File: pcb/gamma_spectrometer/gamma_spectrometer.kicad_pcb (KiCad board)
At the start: 2 copper layers, 255 x 45 mm, 232 parts, among them J101 DX07S024WJ3R400, Q201 IRLML0040, Q401 MMBTA42, Q402 MMBTA42, Q403 MMBTA42, T201 ATB322524-0110-T000, U101 LP5907MFX-3.3, U102 AMS1117-3.3, U103 FT231XQ, U104 TPS60400DBV, U201 max1847eee+, U202 TL431, U301 REF35250QDBVR, U302 STM32G474MET6, U303 W25Q64JVSSIQ, U402 ADA4817-1ARDZ, Y301 ABM8G-16.000MHZ-4Y-T3

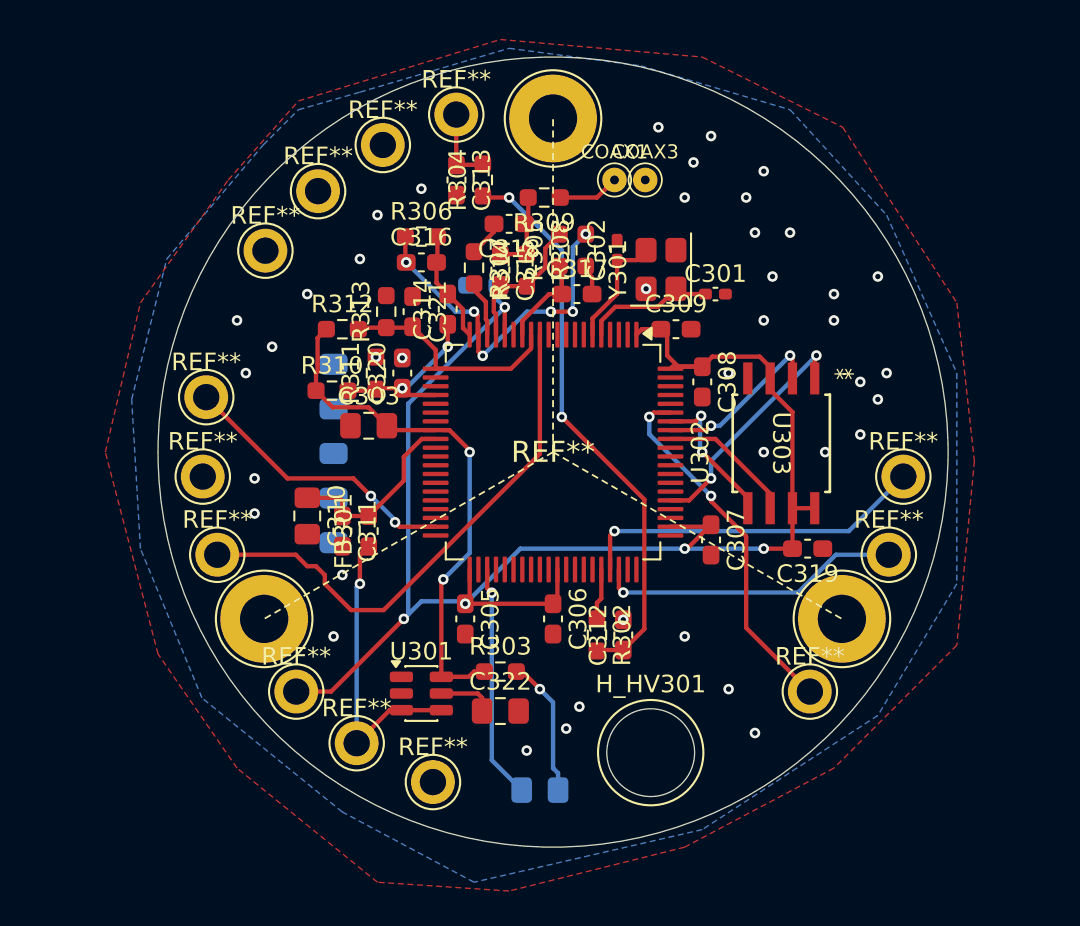
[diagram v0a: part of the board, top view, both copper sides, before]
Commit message: pcb: земля МК подключена, C320 удалён, C314/C317 → 1 мкФ, SWD-пятаки убраны
Плата МК:
- все GND-выводы U302 подключены (15, 27/VSSA, 40, 50 висели);
  зона GND на F.Cu: зазор 0.5 → 0.25 мм, зазор термобарьера → 0.2 мм;
  GND-виа 41 → 97. Остаётся: выводы 50 и 61 на одной спице (starved_thermal).
- TP_SWD301 удалён: прошивка — проводами к выводам 63/64/7 U302.

Схема МК (ревью REVIEW_critic_2026-09-15, находки 1.1 и 1.3, вариант V2):
- C320 удалён (100 нФ на PB0 делил сигнал ×0.5 вместе с C314);
- C314, C317: 100 нФ → 1 мкФ (CC0603JRX7R7BB105), τ связей ~1 мс.

USB-плата: J101 на проектной копии футпринта USB-C (экран на GND).

Co-Authored-By: Claude Opus 5 (1M context) <noreply@anthropic.com>
Claude-Session: https://claude.ai/code/session_018uEKxzknn1WsQbGcTkkQF5
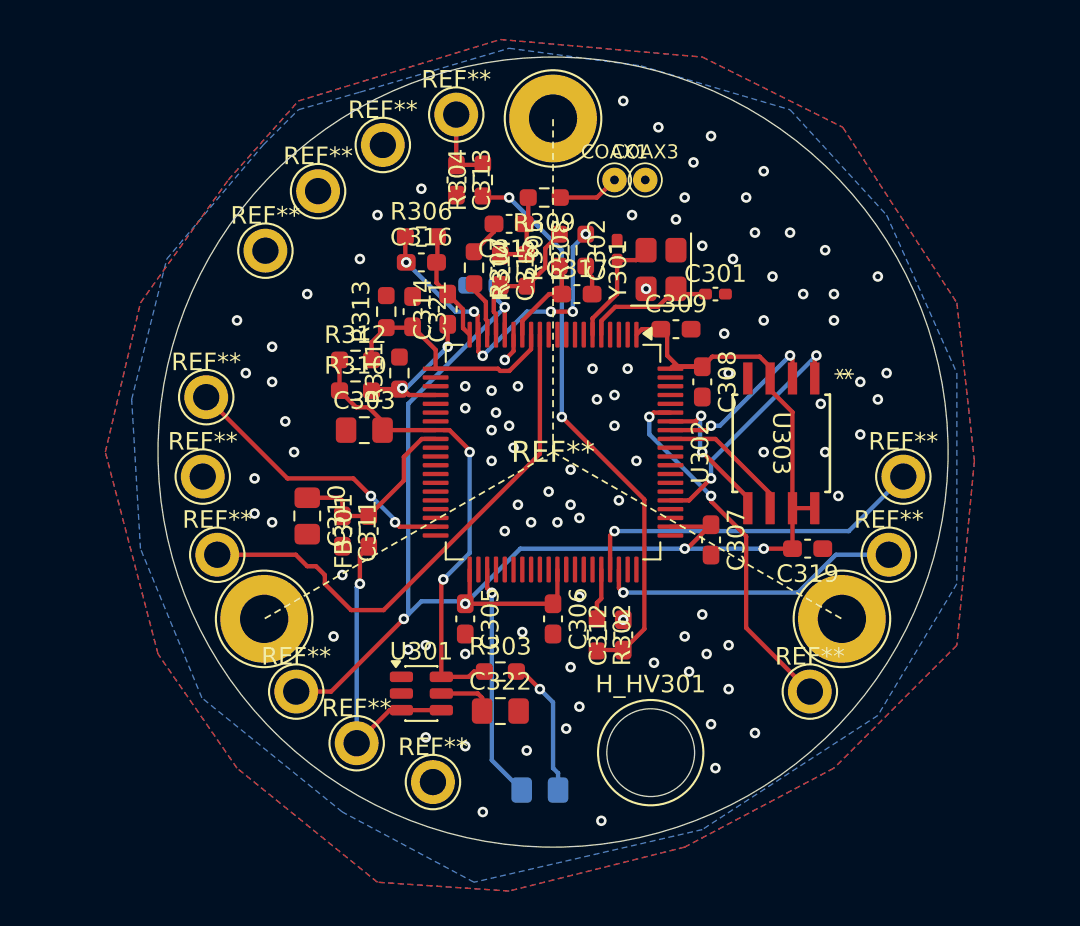
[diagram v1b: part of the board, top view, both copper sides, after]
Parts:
- removed C320: 0.1uF, Capacitor_SMD:C_0603_1608Metric_Pad1.08x0.95mm_HandSolder
- removed TP_SWD301: TP_SWD_5x0805, TP_SWD_5x0805
- C314, C317: value 0.1uF -> 1uF
- moved R312 1.90 mm to (228.8, 94.8)
- moved R310 1.34 mm to (228.8, 96.5)
- moved R311 1.34 mm to (231.2, 95.5)
- moved C303 0.35 mm to (229.2, 98.8)
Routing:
- net Net-(U301-VREF): track 29.6 -> 26.6 mm
- net GND: track 16.9 -> 18.6 mm, vias 98 -> 152
- net Net-(U302-PB0): track 10.4 -> 9.03 mm
- net Net-(U302-PA1): track 12.8 -> 13.5 mm

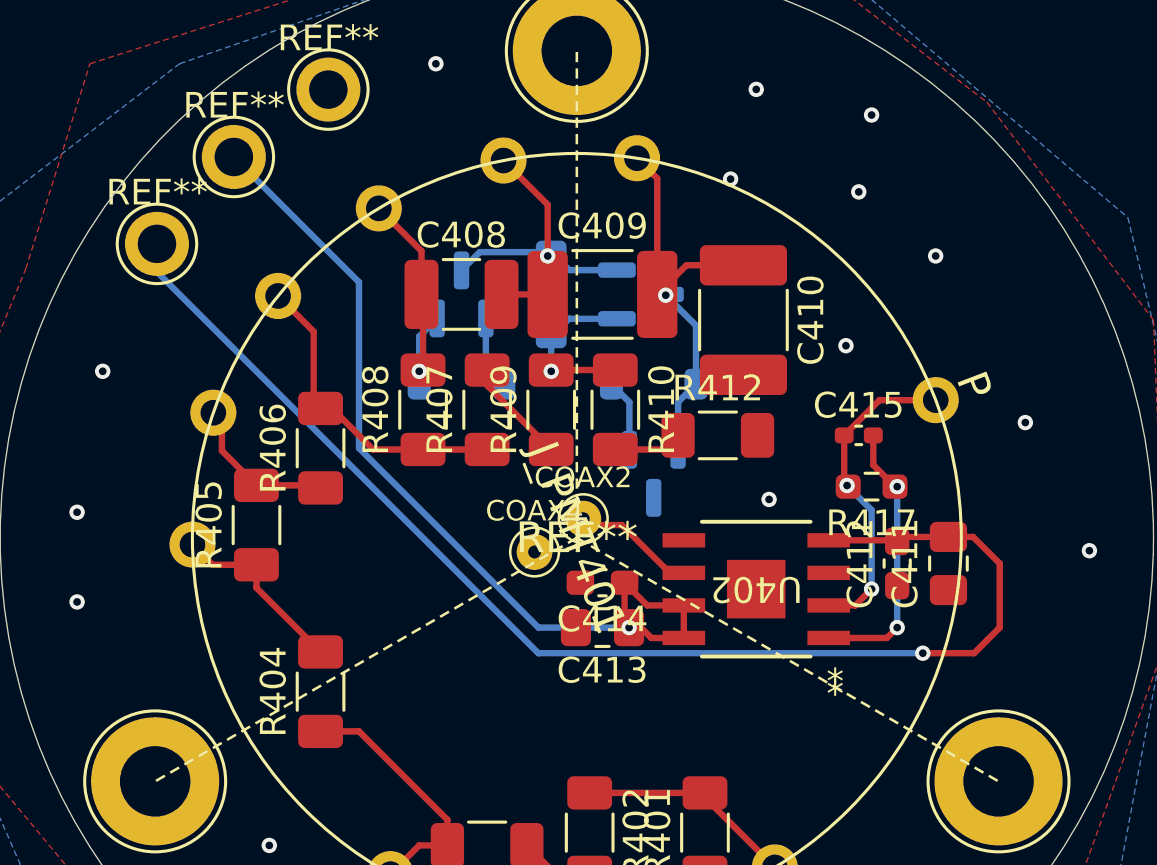
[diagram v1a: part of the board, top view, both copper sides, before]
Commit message: pcb: делитель — R411 22 Ом на выходе TIA, +IN U402 на земле, обратная связь короче
- R411 = 22 Ом (RC0402FR-0722RL, 0402) между выводом 6 U402 и AMP_OUT, вплотную к
  выводу: R_SNUB против генерации TIA на ёмкостную нагрузку (кабель + вход шейпера).
- Вывод 3 U402 (+IN, опорная земля TIA) не был подключён — виа в паде на GND B.Cu.
- R417/C415 перенесены к выводам 1–2: петля обратной связи короче,
  паразитная C(анод↔FB) 0.13–0.22 → 0.05–0.09 пФ.
- Заливка перезалита; DRC по делителю: 0 нарушений зазора, схема↔плата 0.

Co-Authored-By: Claude Opus 5 (1M context) <noreply@anthropic.com>
Claude-Session: https://claude.ai/code/session_018uEKxzknn1WsQbGcTkkQF5
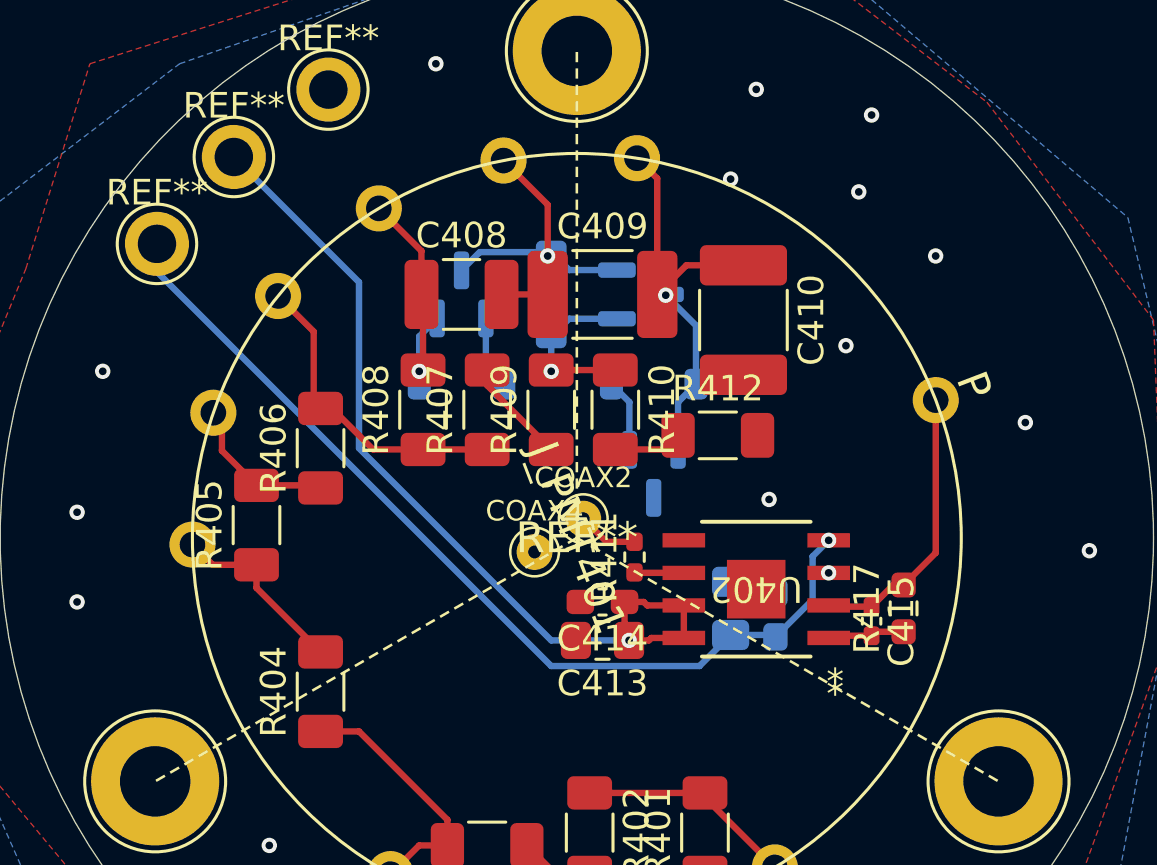
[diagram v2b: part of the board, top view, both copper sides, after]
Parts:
- added R411: 22, Resistor_SMD:R_0402_1005Metric_Pad0.72x0.64mm_HandSolder, F.Cu at (312.2, 100.8)
- C411, C412: moved to B.Cu
- moved C411 8.68 mm to (316.0, 102.8), turned to -90 degrees
- moved C415 7.27 mm to (321.5, 103.2), turned to -90 degrees
- moved C412 5.15 mm to (317.8, 103.0), turned to -90 degrees
- moved R417 4.91 mm to (322.8, 102.8), turned to 90 degrees
- moved C414 0.75 mm to (311.0, 102.5)
- moved C413 0.50 mm to (311.0, 104.0)
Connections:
- U402 pad 6: AMP_OUT -> Net-(U402-OUT)
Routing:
- net −5V_A: track 63.7 -> 50.3 mm
- net FeedBack: track 10.7 -> 3.02 mm, vias 2 -> 0
- net AMP_OUT: track 8.30 -> 5.88 mm
- net Net-(U402-OUT): track 0.00 -> 1.93 mm
- net /Divider_Board/P: track 12.6 -> 11.0 mm, vias 2 -> 0
- net GND: vias 152 -> 153

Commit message: pcb: Q201 IRLML0040 → IRLML0060 (60 В) — запас по выбросу стока
Ключ обратноходового преобразователя ВВ-платы: та же посадка SOT-23 и
распиновка (1-G, 2-S, 3-D). Пик на стоке по расчёту 38.8 В типично,
43–45 В в худшем случае — у IRLML0040 (40 В, лавина не нормирована)
запаса не было. Снаббер BAS516 + C208 + 2×BZT52C18 без изменений.
Схема↔плата: 0 расхождений.

Co-Authored-By: Claude Opus 5 (1M context) <noreply@anthropic.com>
Claude-Session: https://claude.ai/code/session_018uEKxzknn1WsQbGcTkkQF5
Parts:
- Q201: value IRLML0040 -> IRLML0060
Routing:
- net GND: vias 153 -> 164
- net (no net): vias 0 -> 1
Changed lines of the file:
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@@
 			)
 		)
-		(property "Value" "IRLML0040"
+		(property "Value" "IRLML0060"
 			(at 0 2.4 0)
 			(layer "F.Fab")
@@
 			)
 		)
-		(property "PN" "IRLML0040"
+		(property "PN" "IRLML0060"
 			(at 0 0 0)
 			(unlocked yes)
@@
 			)
 		)
-		(property "Ссылка на покупку " "https://www.electronshik.ru/item/HOTTECH/IRLML0040"
+		(property "Ссылка на покупку " "https://www.electronshik.ru/item/HOTTECH/IRLML0060"
 			(at 0 0 0)
 			(unlocked yes)
@@
 		(layer "Edge.Cuts")
 	)
+	(via
+		(at 137.5 118)
+		(size 0.6)
+		(drill 0.3)
+		(layers "F.Cu" "B.Cu")
+		(net 0)
+	)
 	(segment
 		(start 173.3625 93)
@@
 	)
 	(via
+		(at 321.25 96.5)
+		(size 0.6)
+		(drill 0.3)
+		(layers "F.Cu" "B.Cu")
+		(free yes)
+		(net 3)
+	)
+	(via
 		(at 173.5 79)
 		(size 0.6)
@@
 	)
 	(via
+		(at 322 106.5)
+		(size 0.6)
+		(drill 0.3)
+		(layers "F.Cu" "B.Cu")
+		(free yes)
+		(net 3)
+	)
+	(via
 		(at 241 112.25)
 		(size 0.6)
@@
 	)
 	(via
+		(at 319.75 105.75)
+		(size 0.6)
+		(drill 0.3)
+		(layers "F.Cu" "B.Cu")
+		(free yes)
+		(net 3)
+	)
+	(via
 		(at 93 115)
 		(size 0.6)
@@
 	)
 	(via
+		(at 304.75 85)
+		(size 0.6)
+		(drill 0.3)
+		(layers "F.Cu" "B.Cu")
+		(free yes)
+		(net 3)
+	)
+	(via
 		(at 238.25 110.25)
 		(size 0.6)
@@
 	)
 	(via
+		(at 310 84.75)
+		(size 0.6)
+		(drill 0.3)
+		(layers "F.Cu" "B.Cu")
+		(free yes)
+		(net 3)
+	)
+	(via
 		(at 164.5 102)
 		(size 0.6)
@@
 	)
 	(via
+		(at 304.25 102)
+		(size 0.6)
+		(drill 0.3)
+		(layers "F.Cu" "B.Cu")
+		(free yes)
+		(net 3)
+	)
+	(via
 		(at 166 108)
 		(size 0.6)
@@
 	)
 	(via
+		(at 305 103.75)
+		(size 0.6)
+		(drill 0.3)
+		(layers "F.Cu" "B.Cu")
+		(free yes)
+		(net 3)
+	)
+	(via
 		(at 235 116.75)
 		(size 0.6)
@@
 	)
 	(via
+		(at 329.25 104.5)
+		(size 0.6)
+		(drill 0.3)
+		(layers "F.Cu" "B.Cu")
+		(free yes)
+		(net 3)
+	)
+	(via
 		(at 167 121)
 		(size 0.6)
@@
 	)
 	(via
+		(at 320.5 90.25)
+		(size 0.6)
+		(drill 0.3)
+		(layers "F.Cu" "B.Cu")
+		(free yes)
+		(net 3)
+	)
+	(via
 		(at 245.75 112)
 		(size 0.6)
@@
 	)
 	(via
+		(at 315.25 98)
+		(size 0.6)
+		(drill 0.3)
+		(layers "F.Cu" "B.Cu")
+		(free yes)
+		(net 3)
+	)
+	(via
 		(at 238.75 104)
 		(size 0.6)
@@
 		(size 0.6)
 		(drill 0.3)
+		(layers "F.Cu" "B.Cu")
+		(free yes)
+		(net 3)
+	)
+	(via
+		(at 306 105.25)
+		(size 0.6)
+		(drill 0.3)

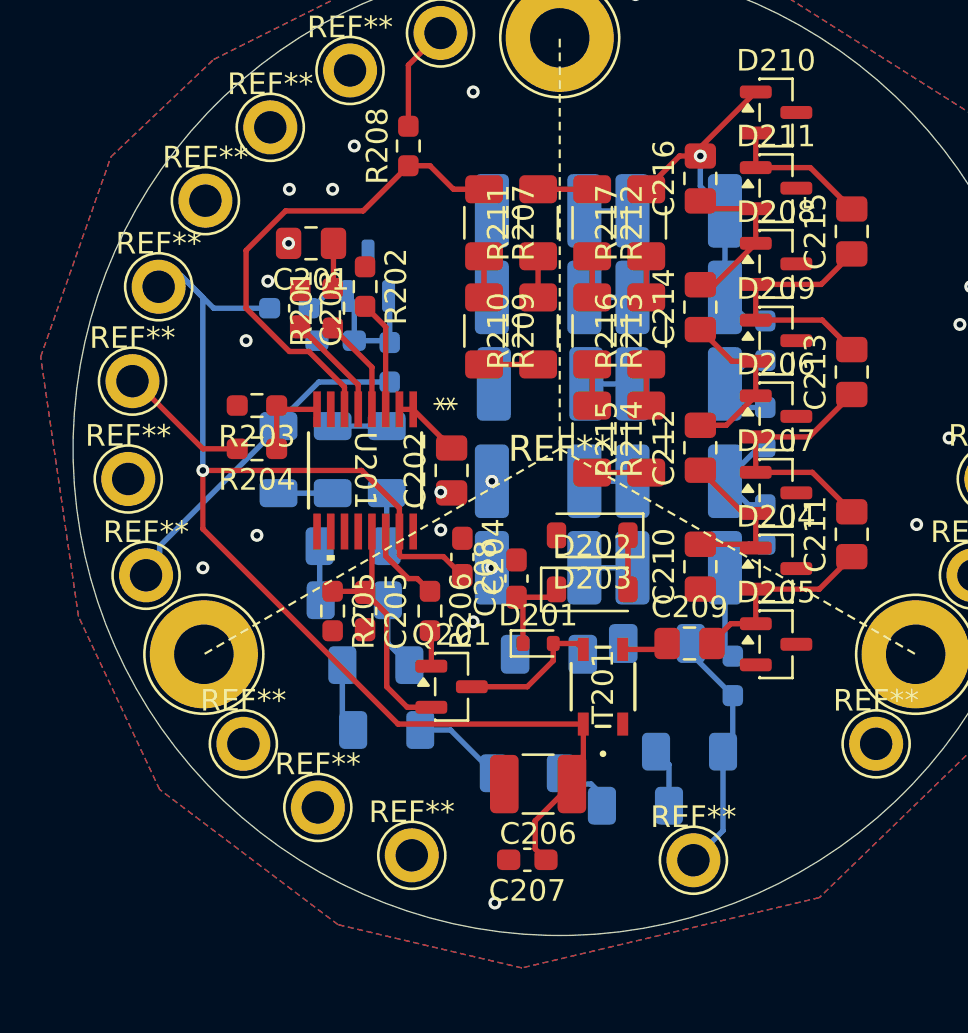
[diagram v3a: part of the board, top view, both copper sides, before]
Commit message: hv: C_COMP2 на плате, перенумерация конденсаторов, проверка земли платы ВВ
Плата и схема (правки пользователя):
- C201 = 22 пФ C0G (C_COMP2) с вывода COMP MAX1847 на GND — по итогам расчёта наводки;
- перенумерация конденсаторов платы ВВ: прежние C201…C217 → C202…C218;
- восстановлена дорожка R201→C202 (без неё запас по фазе падал с 80° до 32°);
- подключён вывод 16 U201 (SYNC) — висел в воздухе;
- сшита земля платы: выводы 10/11/12 MAX1847, R205 и C207 были отделены от вторички,
  умножителя и цепи коррекции, соединялись только через межплатные цанги;
- подключён земляной вывод C211 (возврат умножителя).
Итог по DRC: нарушений зазоров 23 → 4, разрывов земли на плате ВВ — 0.

Документация:
- обновлены все обозначения под новую нумерацию (доки, BOM, шпаргалка, скрипты расчёта);
- C209 (снаббер, 10 нФ) в BOM на 50 В, а узел под ним на 35.7 В с пиками 38–45 В: нужен 100 В;
- C210–C217 (1 нФ 500 В): размах на ступень 310…385 В, запас 1.3× при уставке 1500 В
  (прежняя оценка «189 В» шла из ошибочных 8 ступеней);
- корпуса в BOM платы ВВ приведены к реальным (0603/0805 вместо 0402);
- .net перевыгружен: 178 компонентов.

Осталось: дорожка Net-(C18a201-Pad2) не доходит 0.588 мм до пада C18a201.2 (ВЧ-фильтр
выхода разомкнут), 4 ВВ-зазора, терморазгрузка C202, шелкография.

Co-Authored-By: Claude Opus 5 (1M context) <noreply@anthropic.com>
Claude-Session: https://claude.ai/code/session_018uEKxzknn1WsQbGcTkkQF5
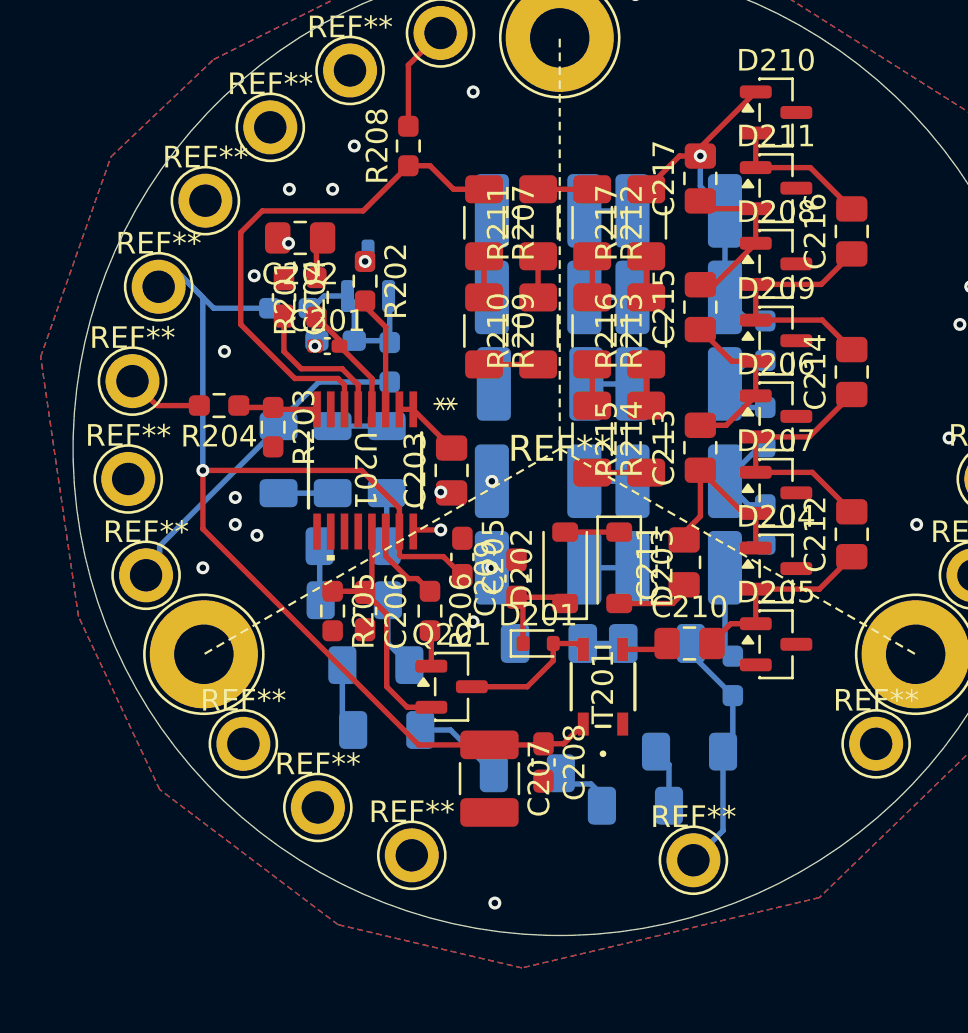
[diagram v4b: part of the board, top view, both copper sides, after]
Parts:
- added C201: 22pF, Capacitor_SMD:C_0402_1005Metric_Pad0.74x0.62mm_HandSolder, F.Cu at (159.2, 95.2)
- moved C208 4.56 mm to (169.2, 114.5), turned to -90 degrees
- moved R204 2.66 mm to (154.2, 98.0)
- moved C207 2.26 mm to (166.8, 115.2), turned to -90 degrees
- moved D203 1.95 mm to (172.8, 105.5), turned to -90 degrees
- moved D202 1.60 mm to (170.2, 105.5), turned to 90 degrees
- moved R203 1.25 mm to (156.8, 99.0), turned to -90 degrees
- moved C204 0.90 mm to (157.2, 93.0)
- moved R201 0.90 mm to (158.8, 93.0)
- moved C211 0.78 mm to (175.8, 105.2)
- moved C202 0.56 mm to (158.0, 90.2)
- moved C18b201 0.50 mm to (169.5, 109.0)
- moved R202 0.25 mm to (161.0, 92.2)
- renumbered C201 to C202, C202 to C203, C203 to C204, C204 to C205, C205 to C206, C206 to C207, C207 to C208, C208 to C209, C209 to C210, C210 to C211, C211 to C212, C212 to C213, C213 to C214, C214 to C215, C215 to C216, C216 to C217, C217 to C218
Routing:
- net +5V_HV: track 90.3 -> 83.9 mm
- net GND: track 18.6 -> 23.1 mm, vias 164 -> 168
- net HV_ENABLE: track 23.0 -> 19.8 mm
- net Net-(U201-REF): track 4.92 -> 6.59 mm
- net Net-(U201-FB): track 22.8 -> 24.3 mm
- net Net-(C18a201-Pad2): track 0.71 -> 1.88 mm
- net Net-(U201-COMP): track 4.51 -> 5.33 mm
- net Net-(C211-Pad2): track 7.64 -> 8.20 mm

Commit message: pcb: виа в цепях баз Q401/Q403 и земля R_CC102
- Net-(D401-K), Net-(D403-K): сторона резисторов делителя (F.Cu) не была соединена
  со стороной базы транзистора и защитного диода (B.Cu) — буферы Dy6 и Dy8 висели.
  Поставлены виа.
- R_CC102 (5.1 кОм на CC USB-C): земляной вывод не цеплялся к заливке — прибор получал
  бы питание от USB-C↔USB-C только в одной ориентации штекера. Подключён.

Проверка: DRC каждой платы отдельной копией (вырезка остальных) — разрывов на уровне
выводов нет ни на одной из четырёх плат; полный DRC — новых нарушений нет.

Co-Authored-By: Claude Opus 5 (1M context) <noreply@anthropic.com>
Claude-Session: https://claude.ai/code/session_018uEKxzknn1WsQbGcTkkQF5
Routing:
- net Net-(D403-K): vias 0 -> 1
- net Net-(D401-K): vias 0 -> 1
- net GND: vias 168 -> 170
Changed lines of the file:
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@@
 	)
 	(via
+		(at 94.5 96)
+		(size 0.6)
+		(drill 0.3)
+		(layers "F.Cu" "B.Cu")
+		(free yes)
+		(net 3)
+	)
+	(via
 		(at 236 120.5)
 		(size 0.6)
@@
 	)
 	(via
+		(at 96.0875 96)
+		(size 0.6)
+		(drill 0.3)
+		(layers "F.Cu" "B.Cu")
+		(net 3)
+	)
+	(via
 		(at 160.5 86)
 		(size 0.6)
@@
 		(net 76)
 	)
+	(via
+		(at 306.95 93.8)
+		(size 0.6)
+		(drill 0.3)
+		(layers "F.Cu" "B.Cu")
+		(net 76)
+	)
+	(segment
+		(start 306.95 93.8)
+		(end 307.15 94)
+		(width 0.25)
+		(layer "B.Cu")
+		(net 76)
+	)
 	(segment
 		(start 306.45 91.4375)
@@
 	(segment
 		(start 306.45 93.3)
-		(end 307.15 94)
+		(end 306.95 93.8)
 		(width 0.25)
 		(layer "B.Cu")
@@
 		(net 187)
 	)
+	(via
+		(at 312.05 96.25)
+		(size 0.6)
+		(drill 0.3)
+		(layers "F.Cu" "B.Cu")
+		(net 187)
+	)
 	(segment
 		(start 312.05 96.5625)
-		(end 312.05 94.7)
+		(end 312.05 96.25)
 		(width 0.25)
 		(layer "B.Cu")
@@
 		(width 0.25)
 		(layer "B.Cu")
+		(net 187)
+	)
+	(segment
+		(start 312.05 96.25)
+		(end 312.05 94.7)
+		(width 0.25)
+		(layer "B.Cu")
